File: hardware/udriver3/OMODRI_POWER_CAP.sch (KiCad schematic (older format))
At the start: 12 parts, among them J13 Conn_01x02

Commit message: Update of the schematics. Switches on GPIO72 & GPIO84 are missing. J1, J2 & J14 must be merged and connector placement optimized. TCXO must be changed from 20MHz to 25MHz for EtherCAT compatibility. PCB is partially routed in 6-Layers (mainly power supplies and and transistors). 8-Layers will be necessary.
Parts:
- removed C106, C107, C108, C109, C110, C111: 100uF, Capacitor_Tantalum_SMD:CP_EIA-7360-38_Kemet-E, symbol Device:CP
- removed TP30, TP31: TestPoint, TestPoint:TestPoint_Pad_D1.0mm, symbol Connector:TestPoint
- added C114, C115, C116: 22uF, Capacitor_SMD:C_2220_5650Metric, symbol Device:C
- J13: footprint Connector_AMASS:AMASS_XT30PW-M_1x02_P2.50mm_Horizontal -> udriver3:AMASS_XT30PW-M_1x02_P2.50mm_Horizontal
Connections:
- wire segments 25 -> 21
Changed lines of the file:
@@
 $Descr A4 11693 8268
 encoding utf-8
-Sheet 16 17
-Title ""
+Sheet 14 17
+Title "Open MOtor DRiver Initiative (OMODRI)"
 Date ""
-Rev ""
-Comp ""
+Rev "1.0"
+Comp "LAAS/CNRS"
 Comment1 ""
 Comment2 ""
@@
 F 3 "" H 4825 4550 50  0001 C CNN
 	1    4825 4550
-	1    0    0    -1
-$EndComp
-$Comp
-L Connector:TestPoint TP?
-U 1 1 5F9F53FF
-P 6575 4050
-AR Path="/5F310311/5F9F53FF" Ref="TP?"  Part="1"
-AR Path="/5F3255E8/5F9F53FF" Ref="TP?"  Part="1"
-AR Path="/5F387075/5F9F53FF" Ref="TP?"  Part="1"
-AR Path="/5F9F53FF" Ref="TP?"  Part="1"
-AR Path="/5F9E8B4A/5F9F53FF" Ref="TP31"  Part="1"
-F 0 "TP31" H 6525 4350 50  0000 L CNN
-F 1 "TestPoint" H 6525 4250 50  0000 L CNN
-F 2 "TestPoint:TestPoint_Pad_D1.0mm" H 6775 4050 50  0001 C CNN
-F 3 "~" H 6775 4050 50  0001 C CNN
-	1    6575 4050
 	1    0    0    -1
 $EndComp
@@
 $EndComp
 $Comp
-L Connector_Generic:Conn_01x02 J?
-U 1 1 5F9F542A
-P 4625 4050
-AR Path="/5F9F542A" Ref="J?"  Part="1"
-AR Path="/5F9E8B4A/5F9F542A" Ref="J13"  Part="1"
-F 0 "J13" H 4625 4150 50  0000 C CNN
-F 1 "Conn_01x02" H 4675 3850 50  0000 C CNN
-F 2 "Connector_AMASS:AMASS_XT30PW-M_1x02_P2.50mm_Horizontal" H 4625 4050 50  0001 C CNN
-F 3 "https://www.tme.eu/en/Document/ce4077e36b79046da520ca73227e15de/XT30PW%20SPEC.pdf" H 4625 4050 50  0001 C CNN
-	1    4625 4050
-	-1   0    0    -1
-$EndComp
-$Comp
 L power:GND #PWR?
 U 1 1 5F9F5430
@@
 $EndComp
 $Comp
-L Connector:TestPoint TP?
-U 1 1 5F9F5436
-P 4825 3650
-AR Path="/5F310311/5F9F5436" Ref="TP?"  Part="1"
-AR Path="/5F3255E8/5F9F5436" Ref="TP?"  Part="1"
-AR Path="/5F387075/5F9F5436" Ref="TP?"  Part="1"
-AR Path="/5F9F5436" Ref="TP?"  Part="1"
-AR Path="/5F9E8B4A/5F9F5436" Ref="TP30"  Part="1"
-F 0 "TP30" V 4725 3750 50  0000 L CNN
-F 1 "TestPoint" V 4925 3550 50  0000 L CNN
-F 2 "TestPoint:TestPoint_Pad_D1.0mm" H 5025 3650 50  0001 C CNN
-F 3 "~" H 5025 3650 50  0001 C CNN
-	1    4825 3650
-	0    -1   -1   0
-$EndComp
-$Comp
 L power:GND #PWR?
 U 1 1 5F9F543C
@@
 $EndComp
 $Comp
-L Device:CP C?
-U 1 1 5F9F5445
-P 5175 3900
-AR Path="/5F9F5445" Ref="C?"  Part="1"
-AR Path="/5F9E8B4A/5F9F5445" Ref="C106"  Part="1"
-F 0 "C106" H 5250 4025 50  0000 L CNN
-F 1 "100uF" H 5200 3775 50  0000 L CNN
-F 2 "Capacitor_Tantalum_SMD:CP_EIA-7360-38_Kemet-E" H 5213 3750 50  0001 C CNN
-F 3 "https://www.vishay.com/docs/40216/t52.pdf" H 5175 3900 50  0001 C CNN
-F 4 "35V" H 5175 3900 50  0001 C CNN "Rated Voltage"
-F 5 "74-T52M1107M035C0055" H 5175 3900 50  0001 C CNN "Mouser"
-F 6 "T52M1107M035C0055" H 5175 3900 50  0001 C CNN "Part No"
-	1    5175 3900
-	1    0    0    -1
-$EndComp
-$Comp
 L power:GND #PWR?
 U 1 1 5F9F544B
@@
 $EndComp
 $Comp
-L Device:CP C?
-U 1 1 5F9F5454
-P 5175 4300
-AR Path="/5F9F5454" Ref="C?"  Part="1"
-AR Path="/5F9E8B4A/5F9F5454" Ref="C109"  Part="1"
-F 0 "C109" H 5250 4425 50  0000 L CNN
-F 1 "100uF" H 5200 4175 50  0000 L CNN
-F 2 "Capacitor_Tantalum_SMD:CP_EIA-7360-38_Kemet-E" H 5213 4150 50  0001 C CNN
-F 3 "https://www.vishay.com/docs/40216/t52.pdf" H 5175 4300 50  0001 C CNN
-F 4 "35V" H 5175 4300 50  0001 C CNN "Rated Voltage"
-F 5 "74-T52M1107M035C0055" H 5175 4300 50  0001 C CNN "Mouser"
-F 6 "T52M1107M035C0055" H 5175 4300 50  0001 C CNN "Part No"
-	1    5175 4300
-	1    0    0    -1
-$EndComp
-$Comp
-L Device:CP C?
-U 1 1 5F9F545D
-P 5525 3900
-AR Path="/5F9F545D" Ref="C?"  Part="1"
-AR Path="/5F9E8B4A/5F9F545D" Ref="C107"  Part="1"
-F 0 "C107" H 5600 4025 50  0000 L CNN
-F 1 "100uF" H 5550 3775 50  0000 L CNN
-F 2 "Capacitor_Tantalum_SMD:CP_EIA-7360-38_Kemet-E" H 5563 3750 50  0001 C CNN
-F 3 "https://www.vishay.com/docs/40216/t52.pdf" H 5525 3900 50  0001 C CNN
-F 4 "35V" H 5525 3900 50  0001 C CNN "Rated Voltage"
-F 5 "74-T52M1107M035C0055" H 5525 3900 50  0001 C CNN "Mouser"
-F 6 "T52M1107M035C0055" H 5525 3900 50  0001 C CNN "Part No"
-	1    5525 3900
-	1    0    0    -1
-$EndComp
-$Comp
-L Device:CP C?
-U 1 1 5F9F5466
-P 5875 3900
-AR Path="/5F9F5466" Ref="C?"  Part="1"
-AR Path="/5F9E8B4A/5F9F5466" Ref="C108"  Part="1"
-F 0 "C108" H 5950 4025 50  0000 L CNN
-F 1 "100uF" H 5900 3775 50  0000 L CNN
-F 2 "Capacitor_Tantalum_SMD:CP_EIA-7360-38_Kemet-E" H 5913 3750 50  0001 C CNN
-F 3 "https://www.vishay.com/docs/40216/t52.pdf" H 5875 3900 50  0001 C CNN
-F 4 "35V" H 5875 3900 50  0001 C CNN "Rated Voltage"
-F 5 "74-T52M1107M035C0055" H 5875 3900 50  0001 C CNN "Mouser"
-F 6 "T52M1107M035C0055" H 5875 3900 50  0001 C CNN "Part No"
-	1    5875 3900
-	1    0    0    -1
-$EndComp
-$Comp
-L Device:CP C?
-U 1 1 5F9F546F
-P 5525 4300
-AR Path="/5F9F546F" Ref="C?"  Part="1"
-AR Path="/5F9E8B4A/5F9F546F" Ref="C110"  Part="1"
-F 0 "C110" H 5600 4425 50  0000 L CNN
-F 1 "100uF" H 5550 4175 50  0000 L CNN
-F 2 "Capacitor_Tantalum_SMD:CP_EIA-7360-38_Kemet-E" H 5563 4150 50  0001 C CNN
-F 3 "https://www.vishay.com/docs/40216/t52.pdf" H 5525 4300 50  0001 C CNN
-F 4 "35V" H 5525 4300 50  0001 C CNN "Rated Voltage"
-F 5 "74-T52M1107M035C0055" H 5525 4300 50  0001 C CNN "Mouser"
-F 6 "T52M1107M035C0055" H 5525 4300 50  0001 C CNN "Part No"
-	1    5525 4300
-	1    0    0    -1
-$EndComp
-$Comp
-L Device:CP C?
-U 1 1 5F9F5478
-P 5875 4300
-AR Path="/5F9F5478" Ref="C?"  Part="1"
-AR Path="/5F9E8B4A/5F9F5478" Ref="C111"  Part="1"
-F 0 "C111" H 5950 4425 50  0000 L CNN
-F 1 "100uF" H 5900 4175 50  0000 L CNN
-F 2 "Capacitor_Tantalum_SMD:CP_EIA-7360-38_Kemet-E" H 5913 4150 50  0001 C CNN
-F 3 "https://www.vishay.com/docs/40216/t52.pdf" H 5875 4300 50  0001 C CNN
-F 4 "35V" H 5875 4300 50  0001 C CNN "Rated Voltage"
-F 5 "74-T52M1107M035C0055" H 5875 4300 50  0001 C CNN "Mouser"
-F 6 "T52M1107M035C0055" H 5875 4300 50  0001 C CNN "Part No"
-	1    5875 4300
-	1    0    0    -1
-$EndComp
-$Comp
 L power:GND #PWR?
 U 1 1 5F9F547E
@@
 	4825 4150 4825 4550
 Wire Wire Line
-	5175 4550 5175 4450
-Wire Wire Line
-	5175 4150 5175 4050
-Wire Wire Line
-	5525 4550 5525 4450
-Wire Wire Line
-	5525 4150 5525 4050
-Wire Wire Line
-	5875 4550 5875 4450
-Wire Wire Line
-	5875 4150 5875 4050
-Wire Wire Line
 	6225 4550 6225 4450
 Wire Wire Line
@@
 	6225 4100 6225 4050
 Connection ~ 6225 4100
-Wire Wire Line
-	6575 4050 6575 4100
 Connection ~ 6575 4100
 Wire Wire Line
 	6225 3750 6225 3650
 Wire Wire Line
-	6225 3650 5875 3650
-Wire Wire Line
-	5875 3650 5875 3750
-Wire Wire Line
 	5875 3650 5525 3650
 Wire Wire Line
-	5525 3650 5525 3750
-Connection ~ 5875 3650
-Wire Wire Line
 	5525 3650 5175 3650
-Wire Wire Line
-	5175 3650 5175 3750
 Connection ~ 5525 3650
 Wire Wire Line
 	5175 3650 4825 3650
-Wire Wire Line
-	4825 3650 4825 4050
 Connection ~ 5175 3650
-Connection ~ 4825 3650
 Wire Wire Line
 	6325 3650 6225 3650
@@
 Text HLabel 6925 4100 2    50   Output ~ 0
 V_Bus
+$Comp
+L Device:C C114
+U 1 1 5F5A9A1E
+P 5175 4100
+F 0 "C114" H 5225 4200 50  0000 L CNN
+F 1 "22uF" H 5225 4000 50  0000 L CNN
+F 2 "Capacitor_SMD:C_2220_5650Metric" H 5213 3950 50  0001 C CNN
+F 3 "https://product.tdk.com/info/en/catalog/datasheets/mlcc_commercial_midvoltage_en.pdf" H 5175 4100 50  0001 C CNN
+F 4 "445-C5750X7S2A226M280KBCT-ND" H 5175 4100 50  0001 C CNN "DigiKey"
+F 5 "3416277" H 5175 4100 50  0001 C CNN "Farnell"
+F 6 "810-C5750X7S2A226280" H 5175 4100 50  0001 C CNN "Mouser"
+F 7 "C5750X7S2A226M280KB" H 5175 4100 50  0001 C CNN "Part No"
+F 8 "100V" H 5175 4100 50  0001 C CNN "Rated Voltage"
+	1    5175 4100
+	1    0    0    -1
+$EndComp
+$Comp
+L Device:C C115
+U 1 1 5F5AE0E5
+P 5525 4100
+F 0 "C115" H 5575 4200 50  0000 L CNN
+F 1 "22uF" H 5575 4000 50  0000 L CNN
+F 2 "Capacitor_SMD:C_2220_5650Metric" H 5563 3950 50  0001 C CNN
+F 3 "https://product.tdk.com/info/en/catalog/datasheets/mlcc_commercial_midvoltage_en.pdf" H 5525 4100 50  0001 C CNN
+F 4 "445-C5750X7S2A226M280KBCT-ND" H 5525 4100 50  0001 C CNN "DigiKey"
+F 5 "3416277" H 5525 4100 50  0001 C CNN "Farnell"
+F 6 "810-C5750X7S2A226280" H 5525 4100 50  0001 C CNN "Mouser"
+F 7 "C5750X7S2A226M280KB" H 5525 4100 50  0001 C CNN "Part No"
+F 8 "100V" H 5525 4100 50  0001 C CNN "Rated Voltage"
+	1    5525 4100
+	1    0    0    -1
+$EndComp
+$Comp
+L Device:C C116
+U 1 1 5F5AF33B
+P 5875 4100
+F 0 "C116" H 5925 4200 50  0000 L CNN
+F 1 "22uF" H 5925 4000 50  0000 L CNN
+F 2 "Capacitor_SMD:C_2220_5650Metric" H 5913 3950 50  0001 C CNN
+F 3 "https://product.tdk.com/info/en/catalog/datasheets/mlcc_commercial_midvoltage_en.pdf" H 5875 4100 50  0001 C CNN
+F 4 "445-C5750X7S2A226M280KBCT-ND" H 5875 4100 50  0001 C CNN "DigiKey"
+F 5 "3416277" H 5875 4100 50  0001 C CNN "Farnell"
+F 6 "810-C5750X7S2A226280" H 5875 4100 50  0001 C CNN "Mouser"
+F 7 "C5750X7S2A226M280KB" H 5875 4100 50  0001 C CNN "Part No"
+F 8 "100V" H 5875 4100 50  0001 C CNN "Rated Voltage"
+	1    5875 4100
+	1    0    0    -1
+$EndComp
+Wire Wire Line
+	4825 3650 4825 4050
+$Comp
+L Connector_Generic:Conn_01x02 J?
+U 1 1 5F9F542A
+P 4625 4150
+AR Path="/5F9F542A" Ref="J?"  Part="1"
+AR Path="/5F9E8B4A/5F9F542A" Ref="J13"  Part="1"
+F 0 "J13" H 4625 4250 50  0000 C CNN
+F 1 "Conn_01x02" H 4675 3950 50  0000 C CNN
+F 2 "udriver3:AMASS_XT30PW-M_1x02_P2.50mm_Horizontal" H 4625 4150 50  0001 C CNN
+F 3 "https://www.tme.eu/en/Document/ce4077e36b79046da520ca73227e15de/XT30PW%20SPEC.pdf" H 4625 4150 50  0001 C CNN
+	1    4625 4150
+	-1   0    0    1
+$EndComp
+Wire Wire Line
+	5175 3650 5175 3950
+Wire Wire Line
+	5175 4250 5175 4550
+Wire Wire Line
+	5525 3650 5525 3950
+Wire Wire Line
+	5525 4250 5525 4550
+Wire Wire Line
+	5875 3650 5875 3950
+Wire Wire Line
+	5875 4250 5875 4550
+Connection ~ 5875 3650
+Wire Wire Line
+	5875 3650 6225 3650
 $EndSCHEMATC

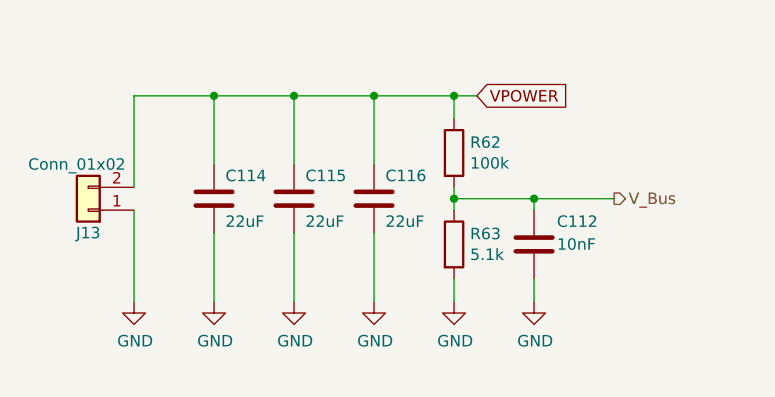
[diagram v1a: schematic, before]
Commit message: Routing update. All analog and DRV signals are wired. TMS mcu decoupling capacitors are in place.
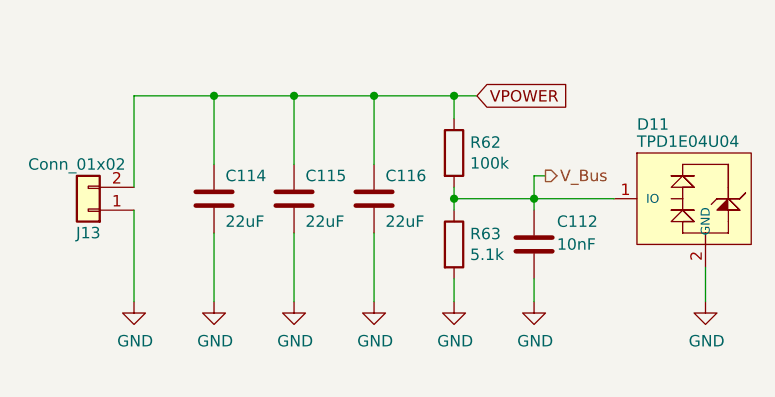
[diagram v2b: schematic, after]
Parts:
- added D11: TPD1E04U04, Diode_SMD:D_0201_0603Metric, symbol omodri_lib:TPD1E04U04
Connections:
- net GND: now also D11.2 (GND)
- net V_Bus: now also D11.1 (IO)
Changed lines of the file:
@@
 Wire Wire Line
 	6925 4100 6575 4100
-Text HLabel 6925 4100 2    50   Output ~ 0
+Text HLabel 6625 4000 2    50   Output ~ 0
 V_Bus
 $Comp
@@
 Wire Wire Line
 	5875 3650 6225 3650
+$Comp
+L omodri_lib:TPD1E04U04 D?
+U 1 1 5F877FCE
+P 7325 4100
+AR Path="/5F5975A7/5F877FCE" Ref="D?"  Part="1"
+AR Path="/5F9E8B4A/5F877FCE" Ref="D11"  Part="1"
+F 0 "D11" H 7025 4425 50  0000 L CNN
+F 1 "TPD1E04U04" H 7025 4350 50  0000 L CNN
+F 2 "Diode_SMD:D_0201_0603Metric" H 7425 4100 50  0001 C CNN
+F 3 "https://www.ti.com/lit/ds/symlink/tpd1e04u04.pdf" H 7425 4100 50  0001 C CNN
+F 4 "296-47224-1-ND" H 7325 4100 50  0001 C CNN "DigiKey"
+F 5 "595-TPD1E04U04DPYR" H 7325 4100 50  0001 C CNN "Mouser"
+F 6 "TPD1E04U04DPYT" H 7325 4100 50  0001 C CNN "Part No"
+	1    7325 4100
+	1    0    0    -1
+$EndComp
+$Comp
+L power:GND #PWR?
+U 1 1 5F877FC3
+P 7325 4550
+AR Path="/5F3A3F16/5F877FC3" Ref="#PWR?"  Part="1"
+AR Path="/5F3A5338/5F877FC3" Ref="#PWR?"  Part="1"
+AR Path="/5F5975A7/5F877FC3" Ref="#PWR?"  Part="1"
+AR Path="/5F9E8B4A/5F877FC3" Ref="#PWR032"  Part="1"
+F 0 "#PWR032" H 7325 4300 50  0001 C CNN
+F 1 "GND" H 7330 4377 50  0000 C CNN
+F 2 "" H 7325 4550 50  0001 C CNN
+F 3 "" H 7325 4550 50  0001 C CNN
+	1    7325 4550
+	1    0    0    -1
+$EndComp
+Wire Wire Line
+	7325 4400 7325 4550
+Wire Wire Line
+	6625 4000 6575 4000
+Wire Wire Line
+	6575 4000 6575 4100
 $EndSCHEMATC

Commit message: Released version, with 4mils/4mils for track width and isolation on outer and inner layers 0.45mm for inner and outer annular ring 0.1mm for finished via drill (for Seeed studio increase to 0.2mm) + USB connector added
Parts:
- D11: footprint Diode_SMD:D_0201_0603Metric -> udriver3:D_0201_0603Metric; DigiKey 296-47224-1-ND -> 296-47862-1-ND; Mouser 595-TPD1E04U04DPYR -> 595-TPD1E04U04DPLT; Part No TPD1E04U04DPYT -> TPD1E04U04DPLT
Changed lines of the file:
@@
 $Descr A4 11693 8268
 encoding utf-8
-Sheet 12 19
+Sheet 19 19
 Title "Open MOtor DRiver Initiative (OMODRI)"
 Date ""
@@
 F 0 "D11" H 7025 4425 50  0000 L CNN
 F 1 "TPD1E04U04" H 7025 4350 50  0000 L CNN
-F 2 "Diode_SMD:D_0201_0603Metric" H 7425 4100 50  0001 C CNN
+F 2 "udriver3:D_0201_0603Metric" H 7425 4100 50  0001 C CNN
 F 3 "https://www.ti.com/lit/ds/symlink/tpd1e04u04.pdf" H 7425 4100 50  0001 C CNN
-F 4 "296-47224-1-ND" H 7325 4100 50  0001 C CNN "DigiKey"
-F 5 "595-TPD1E04U04DPYR" H 7325 4100 50  0001 C CNN "Mouser"
-F 6 "TPD1E04U04DPYT" H 7325 4100 50  0001 C CNN "Part No"
+F 4 "296-47862-1-ND" H 7325 4100 50  0001 C CNN "DigiKey"
+F 5 "595-TPD1E04U04DPLT" H 7325 4100 50  0001 C CNN "Mouser"
+F 6 "TPD1E04U04DPLT" H 7325 4100 50  0001 C CNN "Part No"
 	1    7325 4100
 	1    0    0    -1
